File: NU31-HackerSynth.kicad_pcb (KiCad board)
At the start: 2 copper layers, 180 x 110 mm, 145 parts, among them J2 AudioJack3, J3 Barrel_Jack, J4 AudioJack2_SwitchT, J5 AudioJack2_SwitchT, J6 AudioJack2_SwitchT, J7 Eurorack Power, Q1 BC547, Q2 BC547, Q3 BC547, Q4 BC547, SW1 SW_DPDT, SW2 SW_SPDT, SW3 SW_Rotary_1x8_MP, U1 LM358, U2 LM358, U3 LM358, U4 CD4017, U5 LM358, U6 LM358, U7 LM358

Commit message: Changed slider-switches to push-button and toggle switch, renamed mixer pins to tone
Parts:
- removed JP1, JP2, JP3, JP4, JP5, JP6, JP7, JP8, JP9: Jumper_2_Bridged, Connector_PinHeader_2.54mm:PinHeader_1x02_P2.54mm_Vertical
- added J1: Conn_02x09_Odd_Even, Connector_PinHeader_2.54mm:PinHeader_2x09_P2.54mm_Vertical, F.Cu at (147.0, 54.6)
- J7: moved to F.Cu
- SW1: footprint Button_Switch_THT:SW_CK_JS202011CQN_DPDT_Straight -> SpaceCow:ToggleSwitch_MTS-202_DPDT
- SW2: footprint Button_Switch_THT:SW_Slide_SPDT_Straight_CK_OS102011MS2Q -> SpaceCow:8x8_DPDT_Push_Button
- moved D2 283.2 mm to (340.5, 144.1), turned to 0 degrees
- moved J7 276.7 mm to (336.5, 140.1), turned to 0 degrees
- moved C14 276.6 mm to (330.4, 174.9)
- moved Q1 274.2 mm to (346.7, 161.6), turned to 0 degrees
- moved C13 268.7 mm to (333.8, 134.4)
- moved D4 268.5 mm to (322.4, 117.9), turned to 0 degrees
- moved C1 259.7 mm to (322.3, 160.7)
- moved C2 259.7 mm to (322.3, 165.4)
- moved D6 252.6 mm to (322.4, 122.2), turned to 0 degrees
- moved Q4 250.4 mm to (346.7, 178.5), turned to 0 degrees
- moved C5 247.9 mm to (322.3, 179.7), turned to 0 degrees
- moved R31 242.8 mm to (295.6, 113.5), turned to 0 degrees
- moved D8 235.6 mm to (322.4, 126.4), turned to 0 degrees
- moved Q3 235.5 mm to (346.7, 172.8), turned to 0 degrees
- moved C15 233.0 mm to (330.4, 179.7)
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- renumbered RV13 to RV10, RV14 to RV11, RV10 to RV13, RV11 to RV14
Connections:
- R57 pad 2: /MIX_OUT -> /TONE_OUT
- RV1 pad 1: /MIX_IN -> /TONE_IN
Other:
- board text added: "AUDIO OUT"
- board text added: "CLOCK"
- board text added: "SEQ"
- board text added: "SQUARE"
- board text added: "TRIANGLE"
- board text removed: "--CLOCK--"
- board text removed: "-OSC MIX-"
- board text removed: "OSC MIX"
- board text removed: "OUTPUT"
- board text removed: "SEQUENCER"
- board text removed: "SQ/TRI"

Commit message: Board layout is ready. Also fixed some wrong polarity issues in the schematics
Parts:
- C8: footprint Diode_THT:D_A-405_P10.16mm_Horizontal -> Capacitor_THT:CP_Radial_D5.0mm_P2.50mm
- J2: value AudioJack3 -> GREEN
- J7: moved to B.Cu
- moved D2 287.4 mm to (62.9, 69.5)
- moved C13 285.7 mm to (55.5, 69.5), turned to -90 degrees
- moved J7 280.9 mm to (62.9, 76.8), turned to -90 degrees
- moved C9 279.1 mm to (55.5, 93.5), turned to -90 degrees
- moved Q1 268.5 mm to (91.8, 77.2)
- moved U4 256.8 mm to (84.6, 136.9)
- moved C19 256.1 mm to (85.9, 133.1)
- moved C1 254.4 mm to (88.8, 59.8), turned to 180 degrees
- moved C18 252.7 mm to (92.0, 114.8), turned to 180 degrees
- moved R42 249.4 mm to (52.8, 101.0)
- moved Q3 249.0 mm to (116.7, 77.2)
- moved R46 246.0 mm to (63.0, 109.2), turned to 180 degrees
- moved C2 244.9 mm to (92.0, 81.9), turned to -90 degrees
- moved R45 241.6 mm to (63.0, 105.1), turned to 180 degrees
- moved R43 235.4 mm to (67.3, 105.1)
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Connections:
- U6 pad 4: +VDC -> GND
- U6 pad 8: GND -> +VDC
- U7 pad 4: +VDC -> GND
- U7 pad 8: GND -> +VDC
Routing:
- net +VDC: track 0.00 -> 389.3 mm
- net /SEQ_CV_OUT: track 0.00 -> 264.0 mm
- net Net-(U4-Q7): track 0.00 -> 251.8 mm
- net Net-(U4-Q6): track 0.00 -> 232.2 mm
- net /SEQ_CLOCK_IN: track 0.00 -> 223.2 mm
- net Net-(U4-Q5): track 0.00 -> 175.4 mm
- net Net-(U4-Q4): track 0.00 -> 162.5 mm
- net Net-(U4-Q3): track 0.00 -> 141.5 mm
- net Net-(J5-PadTN): track 0.00 -> 133.6 mm
- net Net-(U4-Q2): track 0.00 -> 116.8 mm
- net Net-(U4-Q1): track 0.00 -> 110.8 mm
- net /OSC1_CV_IN: track 0.00 -> 89.9 mm
- net /DECAY_CV_OUT: track 0.00 -> 87.9 mm
- net /AMP_IN: track 0.00 -> 83.6 mm
- net Net-(RV2-Pad1): track 0.00 -> 77.1 mm
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- added copper zone on B.Cu, net GND
- added copper zone on F.Cu, net GND
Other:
- board text added: "FINE-TUNE"
- board text added: "SEQUENCE LENGTH"

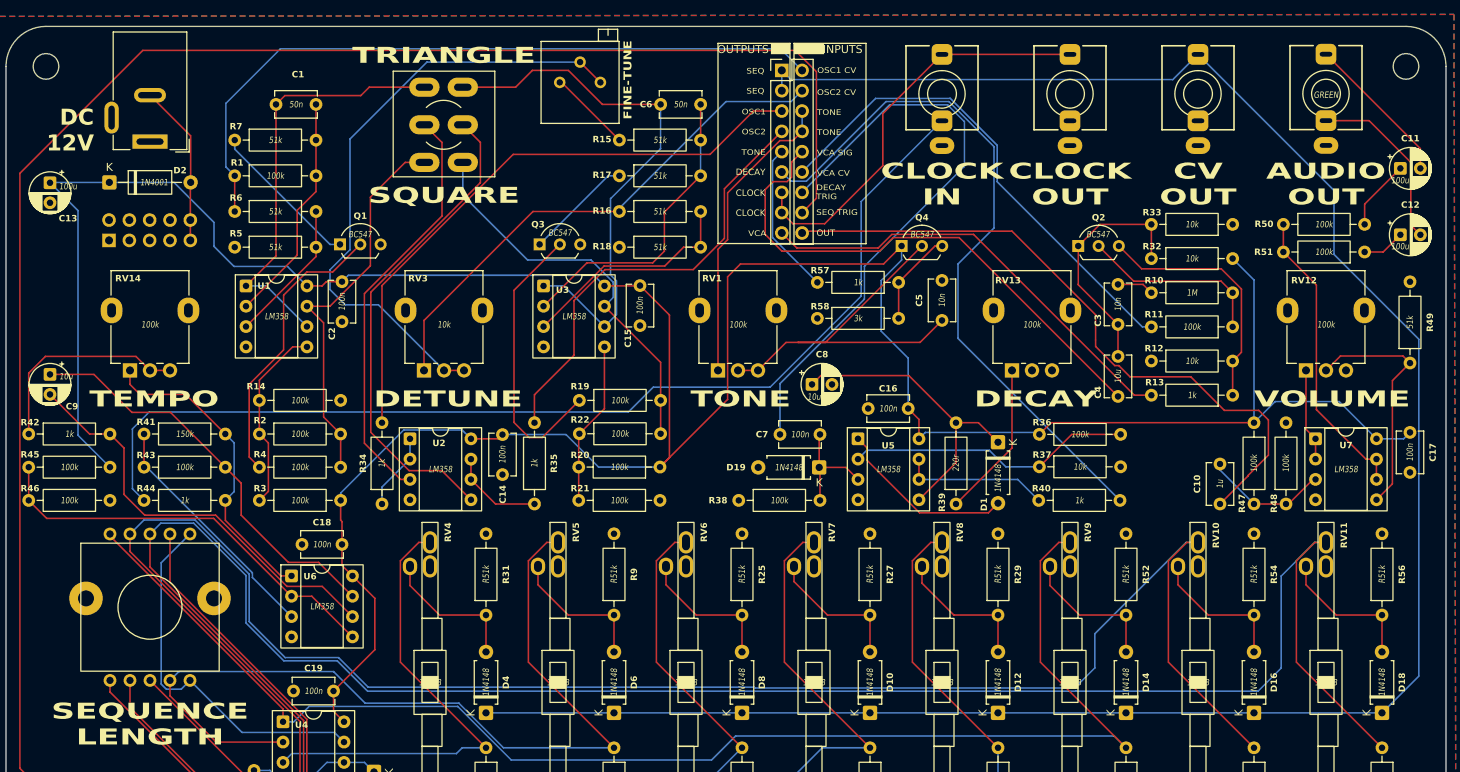
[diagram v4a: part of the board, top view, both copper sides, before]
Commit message: Changed VCC trace width to 0.5mm, changed clearence to 0.2
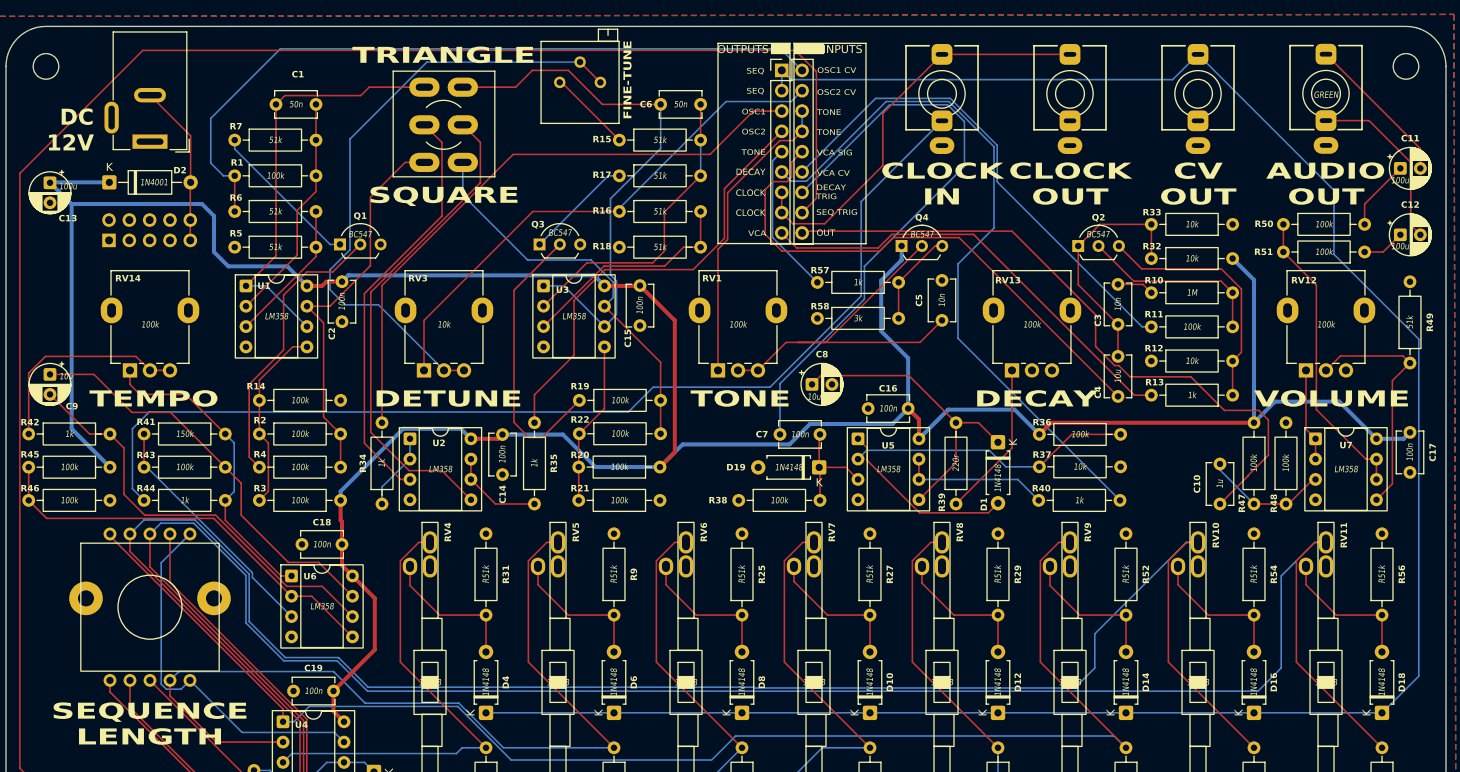
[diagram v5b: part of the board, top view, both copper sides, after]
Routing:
- net +VDC: track 389.3 -> 381.4 mm
- net /OSC1_CV_IN: track 89.9 -> 92.3 mm

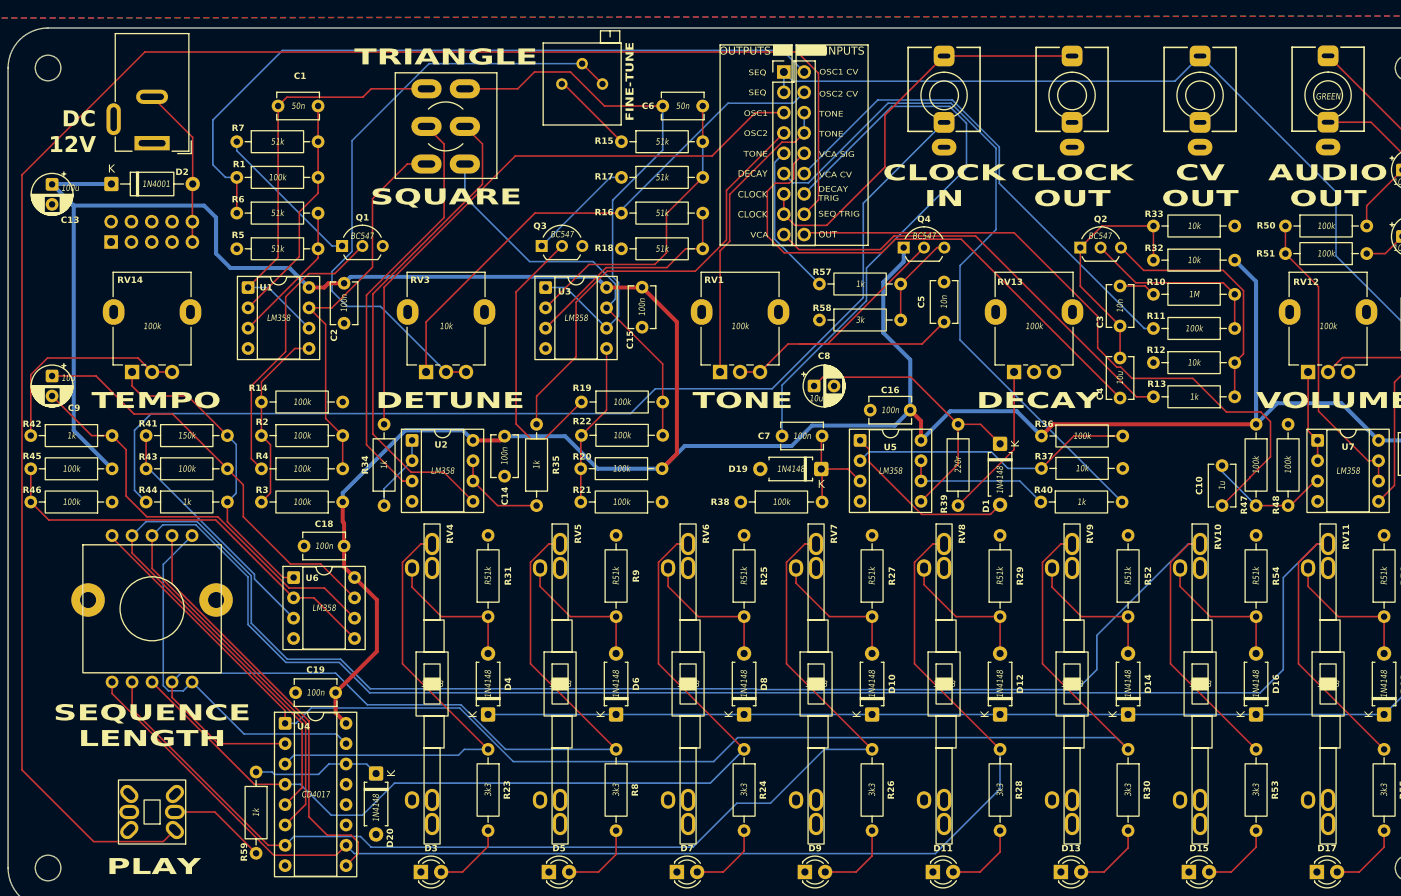
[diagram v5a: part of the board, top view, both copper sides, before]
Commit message: Updated OSC shape switch footprint, optimized routing for decoupling capacitors and ground plane
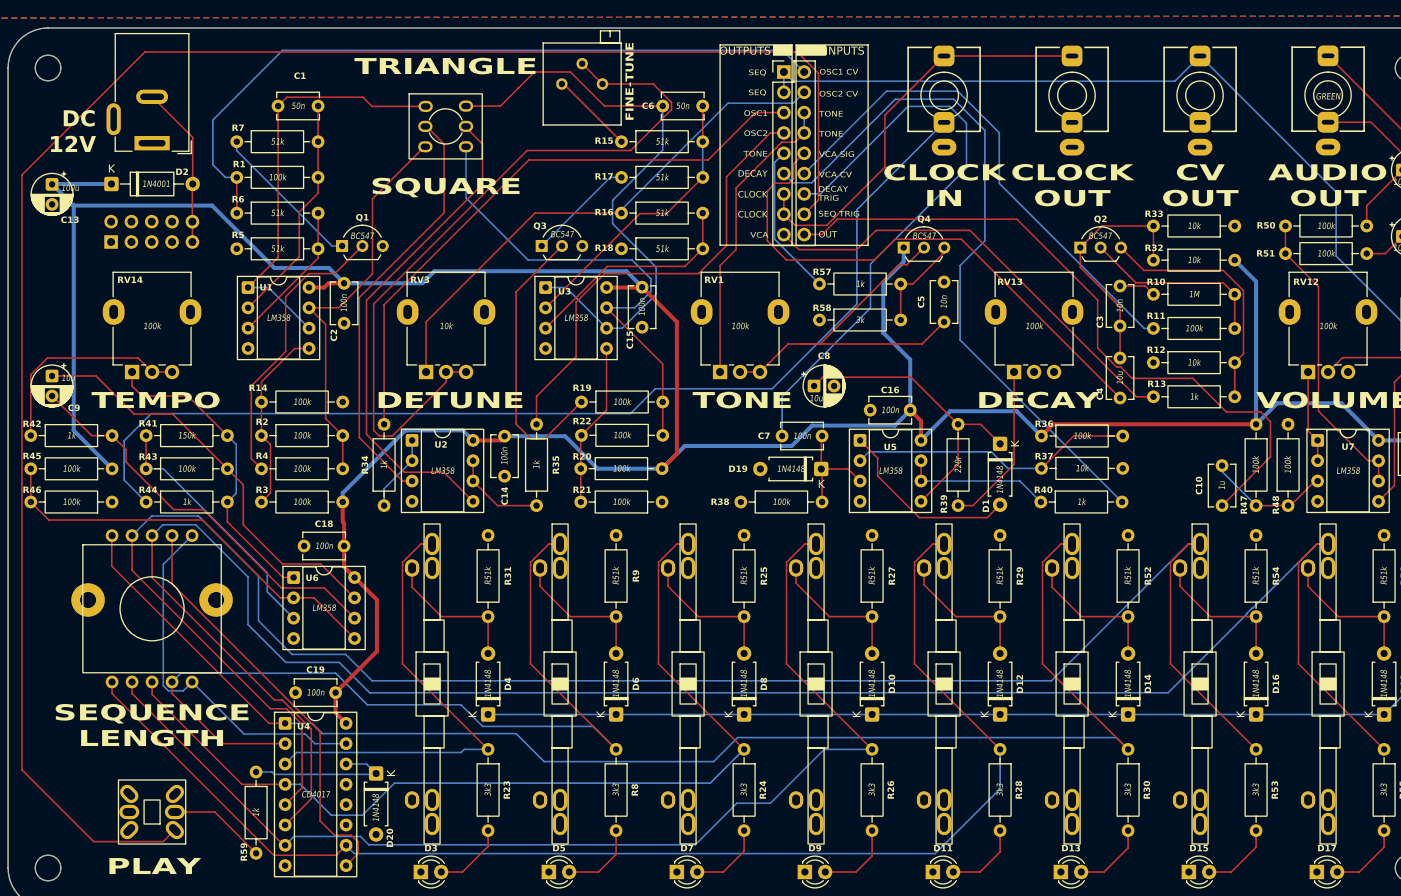
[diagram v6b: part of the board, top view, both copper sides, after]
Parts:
- SW1: footprint SpaceCow:ToggleSwitch_MTS-202_DPDT -> SpaceCow:DPDT-subminiature-toggle
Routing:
- net Net-(RV2-Pad1): track 77.1 -> 93.1 mm
- net /SQ2_OUT: track 49.7 -> 60.5 mm
- net +VDC: track 381.4 -> 388.0 mm
- net /TRI2_OUT: track 68.4 -> 74.3 mm
- net Net-(U4-Q7): track 251.8 -> 246.3 mm
- net Net-(D20-K): track 16.2 -> 19.4 mm
- net Net-(U3A--): track 38.2 -> 35.3 mm
- net /AMP_IN: track 83.6 -> 86.2 mm
- net Net-(U6B--): track 52.7 -> 50.2 mm
- net /VCA_CV_IN: track 62.0 -> 63.9 mm
- net Net-(U4-Q6): track 232.2 -> 230.4 mm
- net /OSC2_OUT: track 55.7 -> 57.1 mm
- net /OSC1_OUT: track 76.2 -> 74.9 mm
- net Net-(U4-Q3): track 141.5 -> 140.2 mm
- net /SQ1_OUT: track 49.0 -> 50.3 mm
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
